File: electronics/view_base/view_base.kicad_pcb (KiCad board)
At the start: 2 copper layers, 110.1 x 99.8 mm, 103 parts, among them J1 BLDC, J2 USB_C_Receptacle_USB2.0, J3 LCD, J4 A, J5 B, J6 Conn_01x28_Socket, J7 Conn_01x28_Socket, J8 Conn_01x03_Socket, J9 Conn_01x04_Socket, Q1 MMBT4403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

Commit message: consult TA about layout
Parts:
- moved C26 0.50 mm to (61.0, 74.0)
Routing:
- net /GPIO1: track 88.2 -> 85.8 mm
- net /GPIO0: track 97.9 -> 96.5 mm
- net /GPIO30: track 97.5 -> 96.7 mm
- net /GPIO12: track 96.4 -> 95.8 mm

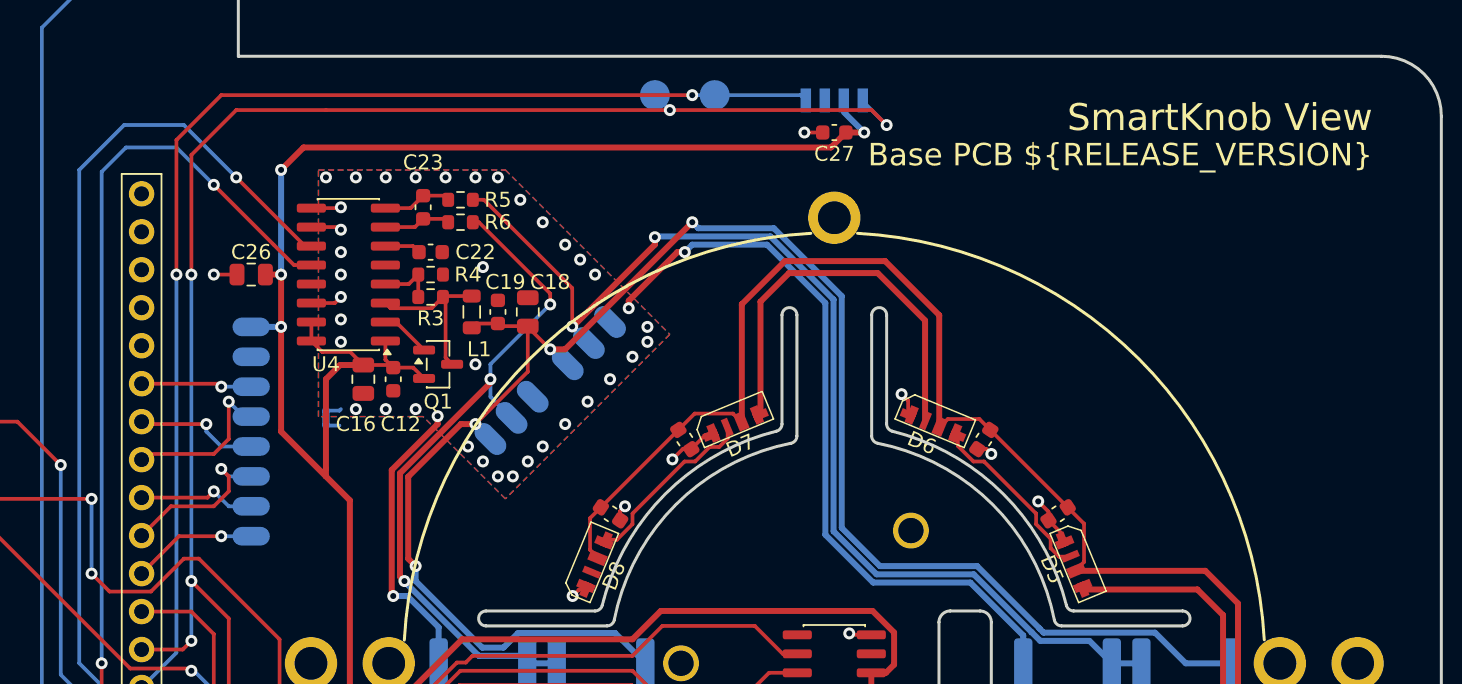
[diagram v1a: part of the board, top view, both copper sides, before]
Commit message: Changed TMC6300 footprint to make vias into thermal reliefs to get rid of drc, added in project title and purdue P
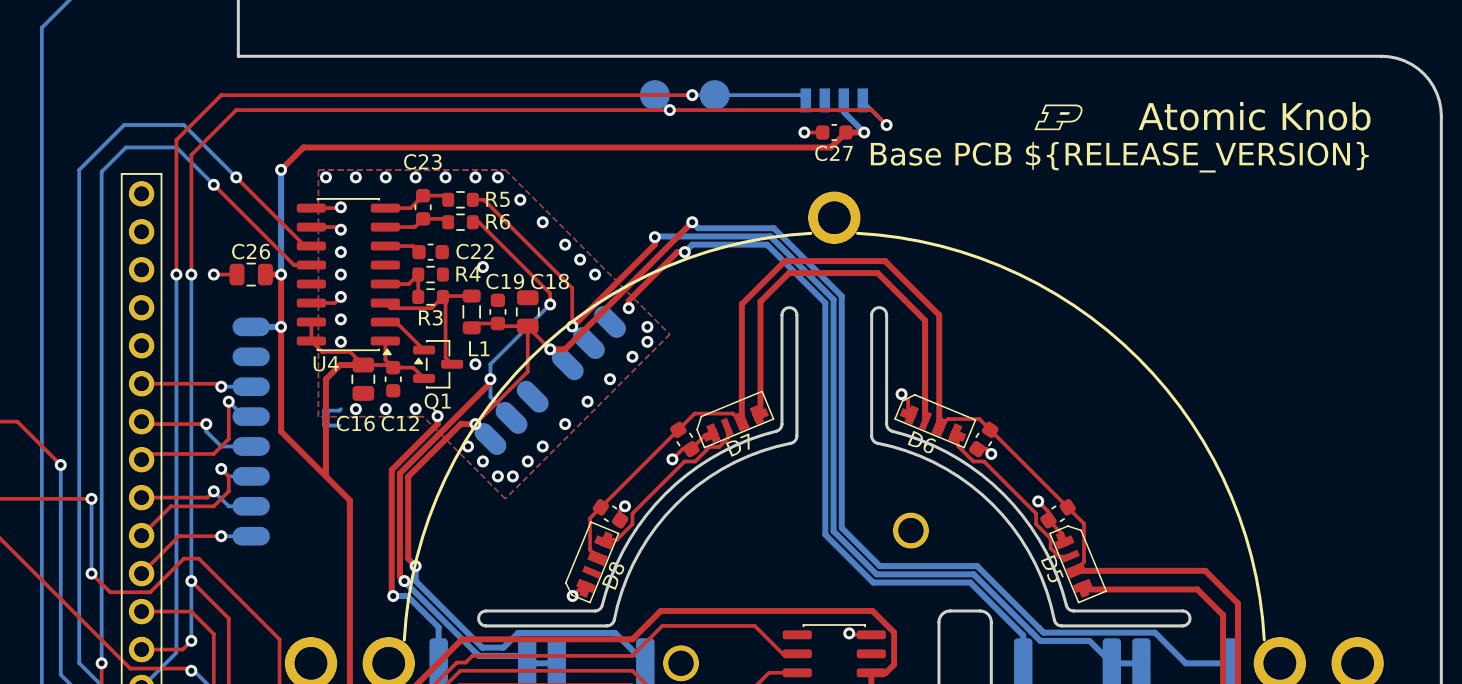
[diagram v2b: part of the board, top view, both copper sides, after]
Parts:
- added G***: LOGO, logos:purdue-small, F.Cu at (115.0, 63.5)
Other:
- board text added: "Atomic Knob"
- board text removed: "SmartKnob View"
